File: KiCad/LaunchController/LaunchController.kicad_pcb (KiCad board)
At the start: 2 copper layers, 120 x 66 mm, 165 parts, among them J1 DC_IN, J10 CONN_EXT_UART, J11 CONN_EXT_I2C_0, J12 CONN_EXT_I2C_1, J13 CONN_EXT_I2C_2, J14 CONN_EXT_I2C_3, J15 CONN_EXT_SPI_0, J16 CONN_EXT_SPI_1, J17 CONN_EXT_SPI_2, J18 CONN_EXT_GPIO_0, J19 CONN_EXT_GPIO_1, J2 CONN_USB, J20 CONN_EXT_GPIO_2, J21 CONN_EXT_GPIO_3, J29 CONN_CONVERTER, J3 USB_B_Micro, J4 CONN_AUDIO, J5 CONN_SPEAKER, J6 CONN_ICSP, J7 L, J8 R, J9 RJ45, Q1 TJ8S06M3L, Q2 2SC3325-Y, Q3 TJ8S06M3L, SW1 SW_RESET, U1 FT232RL, U10 U74HC14, U2 24LC256, U3 INA219BIDCNT, U4 ATMEGA2560-16AUR, U5 INA219BIDCNT, U6 NJM7805SDL1, U7 LTC485CN8#PBF, U8 U74HC14, U9 U74HC14, Y1 HUSG-16.000-20

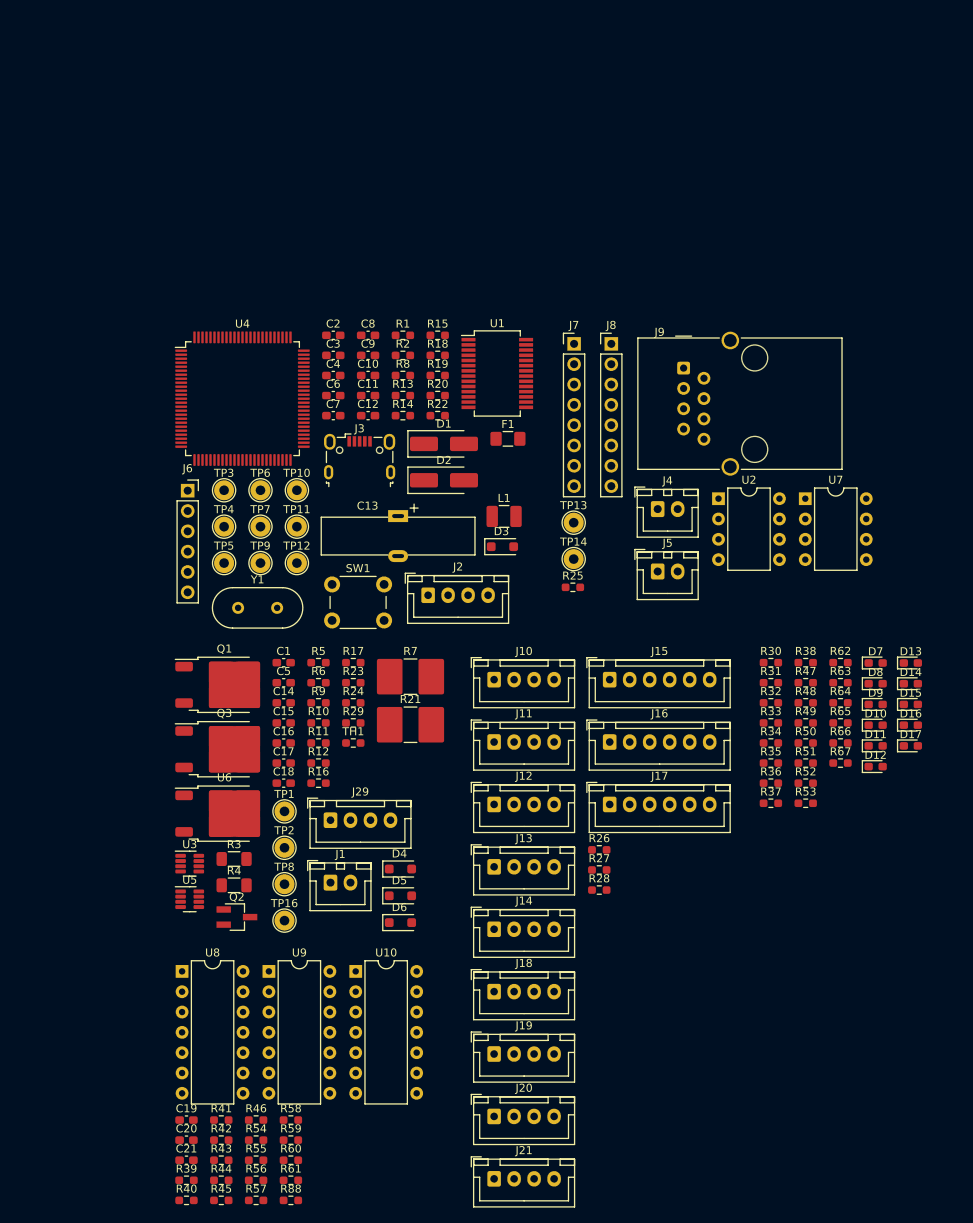
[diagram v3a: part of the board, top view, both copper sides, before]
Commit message: 端子台を選定
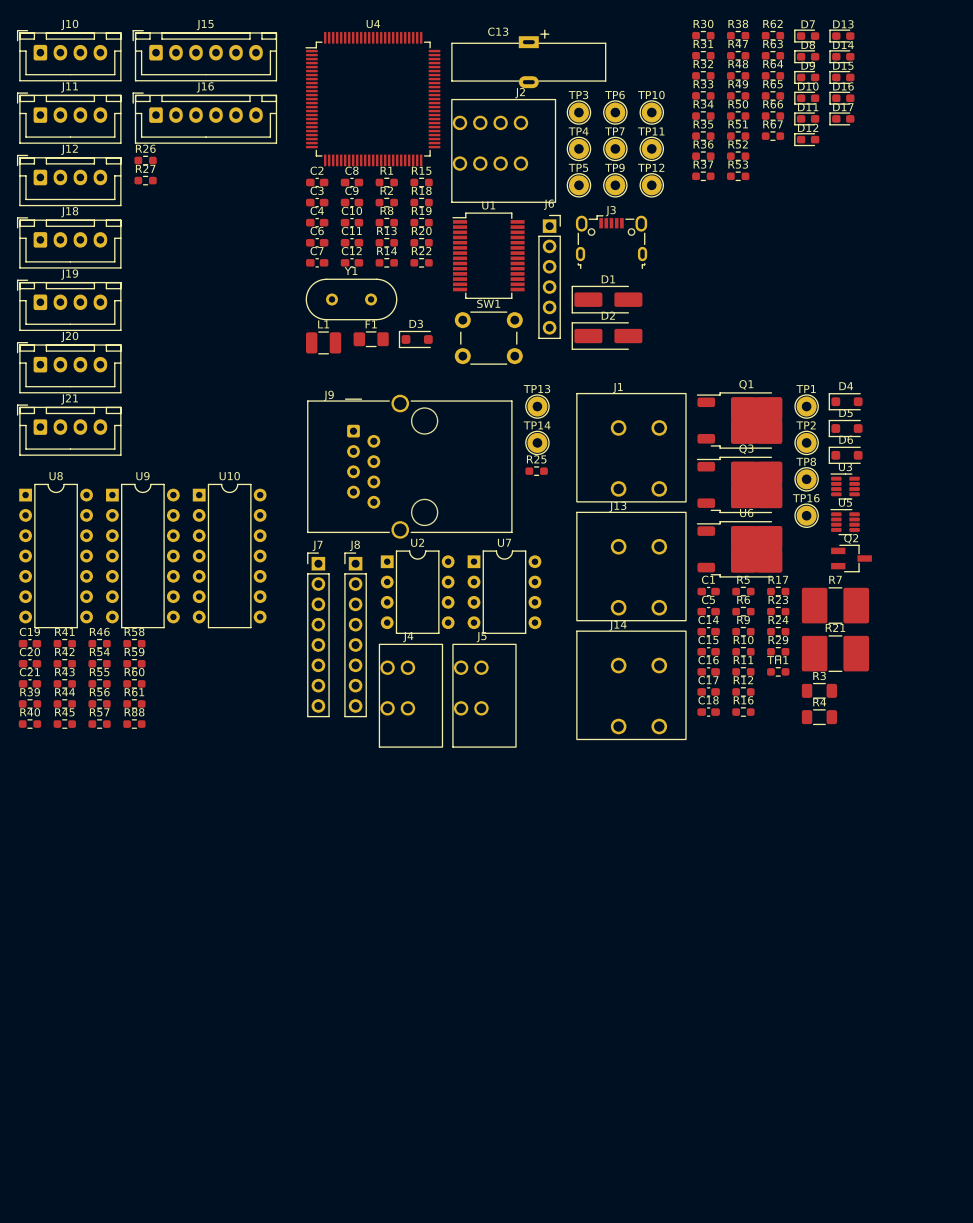
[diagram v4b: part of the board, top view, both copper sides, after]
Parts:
- removed J17: CONN_EXT_SPI_2, Connector_JST:JST_XH_B6B-XH-A_1x06_P2.50mm_Vertical
- removed J29: CONN_CONVERTER, Connector_JST:JST_XH_B4B-XH-A_1x04_P2.50mm_Vertical
- removed R28: 4.7kR, Resistor_SMD:R_0603_1608Metric_Pad0.98x0.95mm_HandSolder
- J1: footprint Connector_JST:JST_XH_B2B-XH-A_1x02_P2.50mm_Vertical -> TSRP_TerminalBlock_Alphaplus:TB411-2-2-E-1
- J13: value CONN_EXT_I2C_2 -> TO_CONVERTER; footprint Connector_JST:JST_XH_B4B-XH-A_1x04_P2.50mm_Vertical -> TSRP_TerminalBlock_Alphaplus:TB411-2-2-E-1
- J14: value CONN_EXT_I2C_3 -> FROM_CONVERTER; footprint Connector_JST:JST_XH_B4B-XH-A_1x04_P2.50mm_Vertical -> TSRP_TerminalBlock_Alphaplus:TB411-2-2-E-1
- J2: footprint Connector_JST:JST_XH_B4B-XH-A_1x04_P2.50mm_Vertical -> TSRP_TerminalBlock_Alphaplus:TB401-1-4-E
- J4, J5: footprint Connector_JST:JST_XH_B2B-XH-A_1x02_P2.50mm_Vertical -> TSRP_TerminalBlock_Alphaplus:TB401-1-2-E
- moved J21 109.8 mm to (-121.0, 98.2)
- moved J18 109.8 mm to (-121.0, 74.8)
- moved J20 109.8 mm to (-121.0, 90.4)
- moved J19 109.8 mm to (-121.0, 82.6)
- moved R26 103.2 mm to (-107.9, 64.9)
- moved R27 103.2 mm to (-107.9, 67.4)
- moved J10 96.7 mm to (-121.0, 51.4)
- moved J12 96.7 mm to (-121.0, 67.0)
- moved J15 96.7 mm to (-106.6, 51.4)
- moved J11 96.7 mm to (-121.0, 59.2)
- moved J16 96.7 mm to (-106.6, 59.2)
- moved U3 94.6 mm to (-20.4, 105.6)
- moved U5 94.6 mm to (-20.4, 110.1)
- moved Q2 88.9 mm to (-19.7, 114.6)
- moved TP16 82.6 mm to (-25.3, 109.3)
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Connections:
- J13 pad 2: I2C_SCL -> TO_CONVERTER
- J14 pad 2: I2C_SCL -> FROM_CONVERTER

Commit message: 拡張スロットを削除
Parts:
- removed J10: CONN_EXT_UART, Connector_JST:JST_XH_B4B-XH-A_1x04_P2.50mm_Vertical
- removed J11: CONN_EXT_I2C_0, Connector_JST:JST_XH_B4B-XH-A_1x04_P2.50mm_Vertical
- removed J12: CONN_EXT_I2C_1, Connector_JST:JST_XH_B4B-XH-A_1x04_P2.50mm_Vertical
- removed J15: CONN_EXT_SPI_0, Connector_JST:JST_XH_B6B-XH-A_1x06_P2.50mm_Vertical
- removed J16: CONN_EXT_SPI_1, Connector_JST:JST_XH_B6B-XH-A_1x06_P2.50mm_Vertical
- removed J18: CONN_EXT_GPIO_0, Connector_JST:JST_XH_B4B-XH-A_1x04_P2.50mm_Vertical
- removed J19: CONN_EXT_GPIO_1, Connector_JST:JST_XH_B4B-XH-A_1x04_P2.50mm_Vertical
- removed J20: CONN_EXT_GPIO_2, Connector_JST:JST_XH_B4B-XH-A_1x04_P2.50mm_Vertical
- removed J21: CONN_EXT_GPIO_3, Connector_JST:JST_XH_B4B-XH-A_1x04_P2.50mm_Vertical
- removed R26, R27: 4.7kR, Resistor_SMD:R_0603_1608Metric_Pad0.98x0.95mm_HandSolder
- added J17: CONN_STATUS_PANEL, TSRP_Connector_Hirose:DF51A-14DP-2DS, F.Cu at (-32.5, 81.2)
- added J22: CONN_PANEL_BAORD_2, TSRP_Connector_Hirose:DF51A-22DP-2DS, F.Cu at (-32.5, 54.3)
- added J23: CONN_PANEL_BAORD_1, TSRP_Connector_Hirose:DF51A-18DP-2DS, F.Cu at (-32.5, 67.8)
- moved U4 247.8 mm to (164.9, 98.2)
- moved R43 125.7 mm to (-39.3, 32.2)
- moved C21 125.7 mm to (-43.6, 32.2)
- moved R41 125.7 mm to (-39.3, 27.2)
- moved R42 125.7 mm to (-39.3, 29.7)
- moved R44 125.7 mm to (-39.3, 34.7)
- moved R45 125.7 mm to (-39.3, 37.3)
- moved R55 125.7 mm to (-34.9, 32.2)
- moved R60 125.7 mm to (-30.6, 32.2)
- moved C19 125.7 mm to (-43.6, 27.2)
- moved C20 125.7 mm to (-43.6, 29.7)
- moved R39 125.7 mm to (-43.6, 34.7)
- moved R40 125.7 mm to (-43.6, 37.3)
- moved R46 125.7 mm to (-34.9, 27.2)
- moved R54 125.7 mm to (-34.9, 29.7)
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
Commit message: 配線終わらん
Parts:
- removed C19, C20, C21: 0.1uF, Capacitor_SMD:C_0603_1608Metric_Pad1.08x0.95mm_HandSolder
- removed J7: L, Connector_PinHeader_2.54mm:PinHeader_1x08_P2.54mm_Vertical
- removed J8: R, Connector_PinHeader_2.54mm:PinHeader_1x08_P2.54mm_Vertical
- removed J9: RJ45, Connector_RJ:RJ45_Wuerth_7499010001A_Horizontal
- removed R39, R40, R41, R42, R43, R44, R45, R46, R54, R55, R56, R57, R58, R59, R60, R61, R88: 1kR, Resistor_SMD:R_0603_1608Metric_Pad0.98x0.95mm_HandSolder
- removed TP10: TP_SDA, TestPoint:TestPoint_THTPad_D2.5mm_Drill1.2mm
- removed TP11: TP_RX0, TestPoint:TestPoint_THTPad_D2.5mm_Drill1.2mm
- removed TP12: TP_TX0, TestPoint:TestPoint_THTPad_D2.5mm_Drill1.2mm
- removed TP13: TP_A, TestPoint:TestPoint_THTPad_D2.5mm_Drill1.2mm
- removed TP14: TP_B, TestPoint:TestPoint_THTPad_D2.5mm_Drill1.2mm
- removed TP3: TP_D+, TestPoint:TestPoint_THTPad_D2.5mm_Drill1.2mm
- removed TP4: TP_D-, TestPoint:TestPoint_THTPad_D2.5mm_Drill1.2mm
- removed TP5: TP_SCK, TestPoint:TestPoint_THTPad_D2.5mm_Drill1.2mm
- removed TP6: TP_MOSI, TestPoint:TestPoint_THTPad_D2.5mm_Drill1.2mm
- removed TP7: TP_MISO, TestPoint:TestPoint_THTPad_D2.5mm_Drill1.2mm
- removed TP9: TP_SCL, TestPoint:TestPoint_THTPad_D2.5mm_Drill1.2mm
- removed U10, U8, U9: U74HC14, Package_DIP:DIP-14_W7.62mm
- added G***: LOGO, LOGO, F.Cu at (136.2, 73.5)
- added G***: LOGO, LOGO, F.Cu at (92.7, 73.5)
- added J10: RJ45, Connector_RJ:RJ45_Wuerth_7499010001A_Horizontal, F.Cu at (95.0, 95.7)
- added U11: DFPlayer, TSRP_Module:DFPlayer-mini, F.Cu at (90.0, 114.1)
- J1, J13, J14, J17, J2, J22, J23, J4, J5: moved to B.Cu
- moved R53 290.5 mm to (176.2, 93.5), turned to 180 degrees
- moved R63 288.3 mm to (176.2, 98.7), turned to 180 degrees
- moved D14 279.1 mm to (176.2, 95.2), turned to 180 degrees
- moved D15 278.9 mm to (176.2, 97.0), turned to 180 degrees
- moved J1 277.2 mm to (173.8, 122.5), turned to 180 degrees
- moved TP2 270.8 mm to (190.7, 123.5)
- moved C1 262.1 mm to (178.7, 117.9), turned to 180 degrees
- moved C2 261.5 mm to (177.2, 88.0), turned to 180 degrees
- moved Q1 260.5 mm to (177.9, 106.8), turned to 90 degrees
- moved R49 260.2 mm to (145.4, 88.5)
- moved R51 259.9 mm to (145.4, 90.5)
- moved TP16 257.7 mm to (182.7, 118.0)
- moved J13 257.6 mm to (158.8, 122.5), turned to 180 degrees
- moved SW1 257.0 mm to (190.4, 110.7), turned to -90 degrees
- moved R65 255.6 mm to (145.4, 85.5)
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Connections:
- net CONN_LED_SAFTEY renamed LED_SAFTEY
- C8 pad 1: Net-(U4-AREF) -> USB_GND
- C8 pad 2: USB_GND -> Net-(U4-AREF)
- D3 pad 2: CTL_RESET -> SW_RESET
- J22 pad 11: CONN_LED_CLOSE -> LED_CLOSE
- J22 pad 13: CONN_LED_IGNITOR -> LED_IGNITOR
- J22 pad 15: CONN_LED_DUMP -> LED_DUMP
- J22 pad 17: CONN_LED_SHIFT -> LED_SHIFT
- J22 pad 19: CONN_LED_SEQUENCE -> LED_SEQUENCE
- J22 pad 21: CONN_LED_POWER -> LED_POWER
- J22 pad 9: CONN_LED_FB_SHIFT -> LED_FB_SHIFT
- Q2 pad 3: CTL_RUN -> SW_RUN
- R13 pad 2: CTL_RESET -> SW_RESET
- R4 pad 2: CTL_RUN -> SW_RUN
- SW1 pad 2: CTL_RESET -> SW_RESET
- U4 pad 25: unconnected-(U4-PB6-Pad25) -> CTL_POWER
- U4 pad 30: CTL_RESET -> SW_RESET
- U4 pad 35: unconnected-(U4-PL0-Pad35) -> LED_LOW_VOLTAGE
- U4 pad 36: unconnected-(U4-PL1-Pad36) -> LED_TASK
- U4 pad 37: unconnected-(U4-PL2-Pad37) -> LED_COM
- U4 pad 38: unconnected-(U4-PL3-Pad38) -> LED_CAUTION
- U4 pad 47: unconnected-(U4-PD4-Pad47) -> LED_POWER
- U4 pad 48: unconnected-(U4-PD5-Pad48) -> LED_SEQUENCE
- U4 pad 49: unconnected-(U4-PD6-Pad49) -> LED_SHIFT
- U4 pad 50: unconnected-(U4-PD7-Pad50) -> LED_DUMP
- U4 pad 51: unconnected-(U4-PG0-Pad51) -> LED_IGNITOR
- U4 pad 52: unconnected-(U4-PG1-Pad52) -> LED_CLOSE
- U4 pad 53: unconnected-(U4-PC0-Pad53) -> LED_FB_SHIFT
- U4 pad 90: unconnected-(U4-PF7-Pad90) -> LED_RS485_RX
- U4 pad 91: unconnected-(U4-PF6-Pad91) -> LED_RS485_TX
- U4 pad 92: unconnected-(U4-PF5-Pad92) -> CTL_RS485_DERE
- U4 pad 93: unconnected-(U4-PF4-Pad93) -> VREF_THERMISTOR
- U4 pad 94: unconnected-(U4-PF3-Pad94) -> VREF_12V
- U4 pad 95: unconnected-(U4-PF2-Pad95) -> VREF_VSW
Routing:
- net LED_5V: track 0.00 -> 362.9 mm, vias 0 -> 11
- net LED_INPUT: track 0.00 -> 160.4 mm, vias 0 -> 5
- net I2C_SCL: track 0.00 -> 147.8 mm, vias 0 -> 4
- net LED_12V: track 0.00 -> 132.5 mm, vias 0 -> 4
- net I2C_SDA: track 0.00 -> 128.8 mm, vias 0 -> 3
- net CTL_RESET: track 0.00 -> 91.0 mm, vias 0 -> 3
- net LED_USB_RX: track 0.00 -> 89.5 mm, vias 0 -> 3
- net LED_LOW_VOLTAGE: track 0.00 -> 86.1 mm, vias 0 -> 4
- net LED_USB_TX: track 0.00 -> 75.5 mm, vias 0 -> 3
- net CTL_POWER: track 0.00 -> 68.7 mm, vias 0 -> 2
- net USB_VBUS: track 0.00 -> 54.2 mm, vias 0 -> 2
- net UART1_RX: track 0.00 -> 53.1 mm, vias 0 -> 1
- net LED_CAUTION: track 0.00 -> 52.7 mm, vias 0 -> 5
- net VREF_THERMISTOR: track 0.00 -> 51.7 mm, vias 0 -> 4
- net Net-(U4-PE1): track 0.00 -> 51.5 mm, vias 0 -> 2
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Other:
- board text added: "+"
- board text added: "-"
- board text added: "12V"
- board text added: "5V"
- board text added: "AUDIO"
- board text added: "Com"
- board text added: "Ctn"
- board text added: "D+"
- board text added: "D-"
- board text added: "DC 15-24V 3.2A MAX"
- board text added: "DC IN"
- board text added: "FROM DCDC"
- board text added: "GND"
- board text added: "Gen 6 GSE Launch Controller Build 1"
- board text added: "ICSP"
- board text added: "INPUT"
- board text added: "LOW"
- board text added: "POWER"
- board text added: "RESET"
- board text added: "Rx"
- board text added: "SPEAKER"
- board text added: "TO DCDC"
- board text added: "Tokai Student Rocket Project"
- board text added: "Tsk"
- board text added: "Tx"
- board text added: "USB"
- board text added: "VBUS"

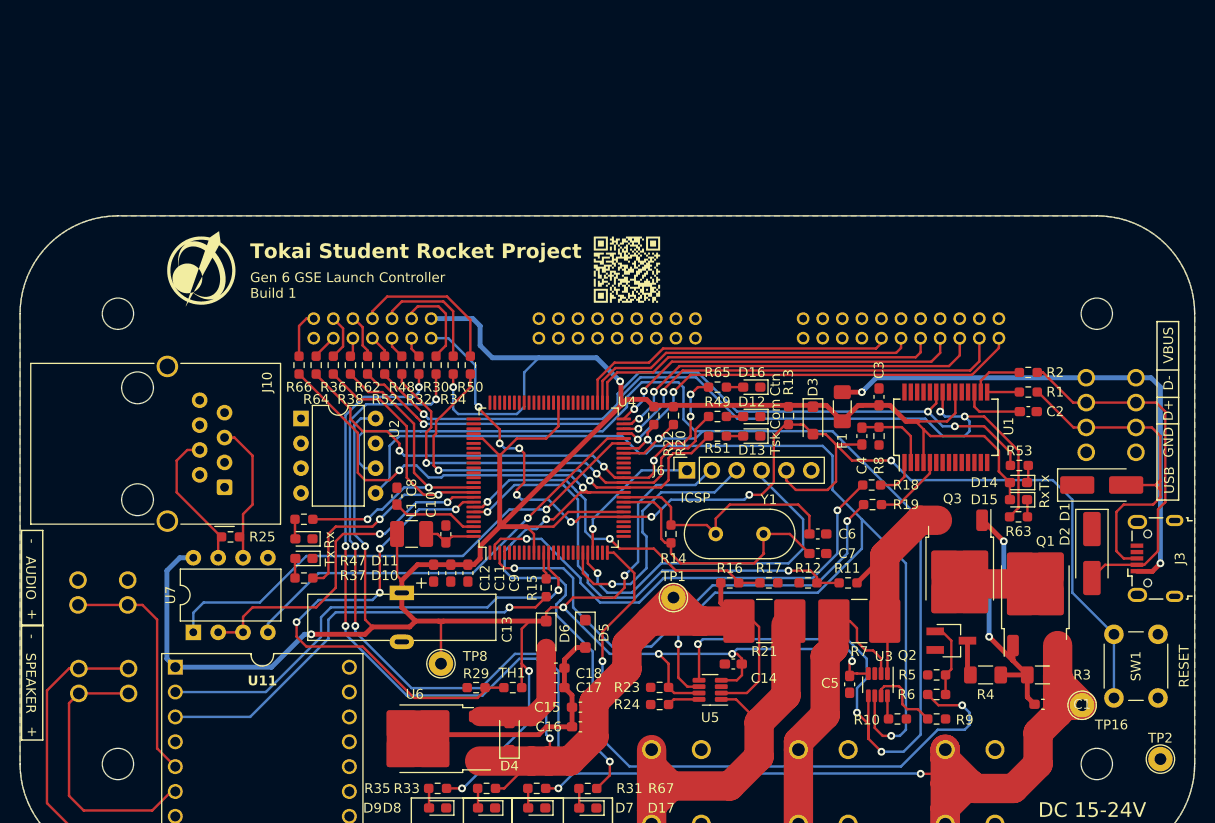
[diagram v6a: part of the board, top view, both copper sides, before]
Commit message: シュミットトリガー無しで部品を配置
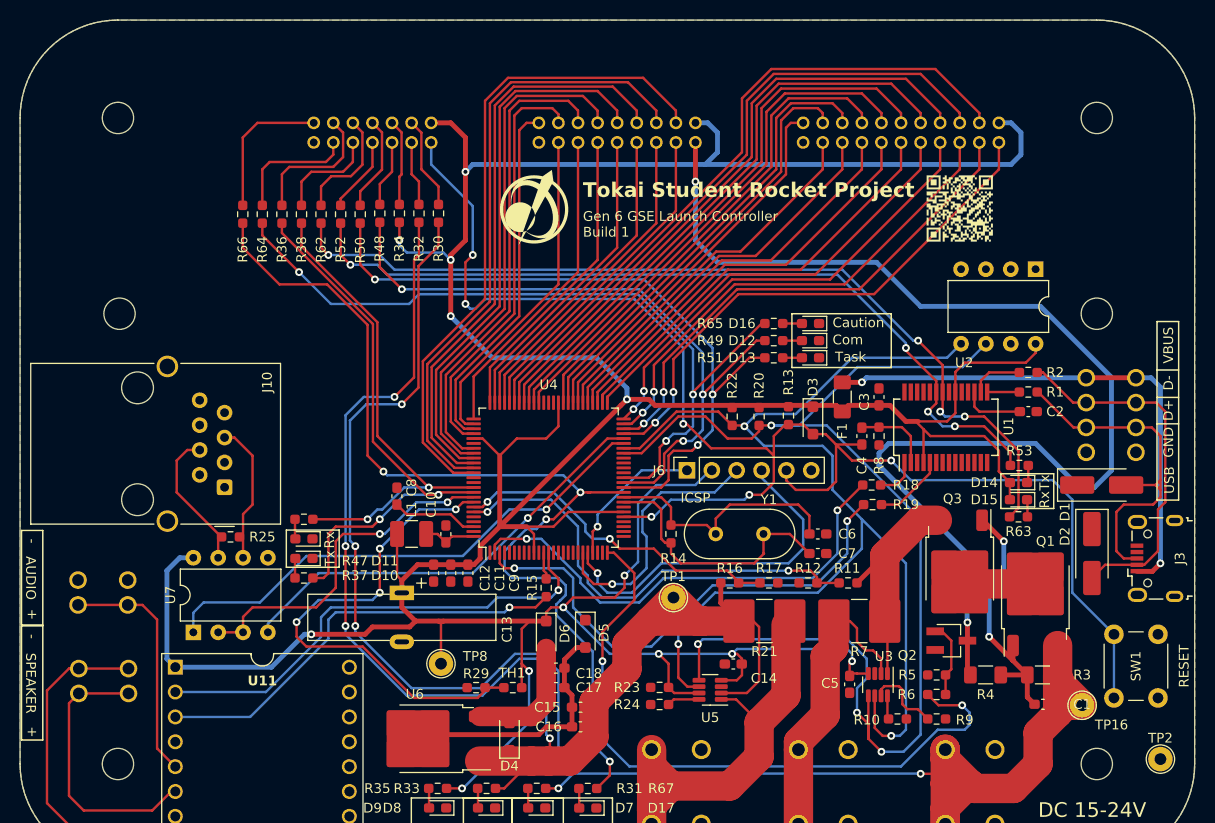
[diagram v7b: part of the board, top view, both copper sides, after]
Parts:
- added REF**: MountingHole_3.2mm_M3, MountingHole:MountingHole_3.2mm_M3, F.Cu at (184.2, 78.0)
- added REF**: MountingHole_3.2mm_M3, MountingHole:MountingHole_3.2mm_M3, F.Cu at (84.3, 78.0)
- moved U2 76.6 mm to (177.9, 73.4), turned to -90 degrees
- moved G*** 34.6 mm to (170.2, 67.2)
- moved G*** 34.6 mm to (126.7, 67.2)
- moved J17 20.0 mm to (104.2, 60.5)
- moved J22 20.0 mm to (154.2, 60.5)
- moved J23 20.0 mm to (127.2, 60.5)
- moved REF** 20.0 mm to (184.2, 58.0)
- moved REF** 20.0 mm to (84.2, 58.0)
- moved R50 19.1 mm to (108.9, 67.8)
- moved R66 16.5 mm to (96.9, 67.8)
- moved R34 16.4 mm to (112.9, 67.7)
- moved R64 16.4 mm to (98.9, 67.8)
- moved R36 16.3 mm to (100.9, 67.8)
- moved R38 16.2 mm to (102.9, 67.8)
- moved R62 16.1 mm to (104.9, 67.8)
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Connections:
- C4 pad 2: CTL_RESET -> SW_RESET
- J22 pad 10: CONN_LED_PURGE -> LED_PURGE
- J22 pad 12: CONN_LED_OPEN -> LED_OPEN
- J22 pad 14: CONN_LED_O2 -> LED_O2
- J22 pad 16: CONN_LED_FILL -> LED_FILL
- J22 pad 18: CONN_LED_EMERGENCY -> LED_EMERGENCY
- J22 pad 2: CONN_LED_FB_PURGE -> LED_FB_PURGE
- J22 pad 3: CONN_LED_FB_CLOSE -> LED_FB_CLOSE
- J22 pad 4: CONN_LED_FB_OPEN -> LED_FB_OPEN
- J22 pad 5: CONN_LED_FB_IGNITOR -> LED_FB_IGNITOR
- J22 pad 6: CONN_FB_LED_O2 -> LED_FB_O2
- J22 pad 7: CONN_LED_FB_DUMP -> LED_FB_DUMP
- J22 pad 8: CONN_LED_FB_FILL -> LED_FB_FILL
- J6 pad 5: CTL_RESET -> SW_RESET
- U4 pad 54: unconnected-(U4-PC1-Pad54) -> LED_FB_DUMP
- U4 pad 55: unconnected-(U4-PC2-Pad55) -> LED_FB_IGNITOR
- U4 pad 56: unconnected-(U4-PC3-Pad56) -> LED_FB_CLOSE
- U4 pad 57: unconnected-(U4-PC4-Pad57) -> LED_FB_PURGE
- U4 pad 58: unconnected-(U4-PC5-Pad58) -> LED_FB_OPEN
- U4 pad 59: unconnected-(U4-PC6-Pad59) -> LED_FB_O2
- U4 pad 60: unconnected-(U4-PC7-Pad60) -> LED_FB_FILL
- U4 pad 65: unconnected-(U4-PJ2-Pad65) -> LED_PURGE
- U4 pad 66: unconnected-(U4-PJ3-Pad66) -> LED_OPEN
- U4 pad 67: unconnected-(U4-PJ4-Pad67) -> LED_O2
- U4 pad 68: unconnected-(U4-PJ5-Pad68) -> LED_FILL
- U4 pad 69: unconnected-(U4-PJ6-Pad69) -> LED_EMERGENCY
- U4 pad 70: unconnected-(U4-PG2-Pad70) -> LED_SAFTEY
- U4 pad 71: unconnected-(U4-PA7-Pad71) -> SW_SAFETY
- U4 pad 72: unconnected-(U4-PA6-Pad72) -> SW_EMERGENCY_STOP
- U4 pad 73: unconnected-(U4-PA5-Pad73) -> SW_CONFIRM_2
- U4 pad 74: unconnected-(U4-PA4-Pad74) -> SW_SHIFT
- U4 pad 75: unconnected-(U4-PA3-Pad75) -> SW_DUMP
- U4 pad 76: unconnected-(U4-PA2-Pad76) -> SW_IGNITOR
- U4 pad 77: unconnected-(U4-PA1-Pad77) -> SW_CLOSE
- U4 pad 78: unconnected-(U4-PA0-Pad78) -> SW_PURGE
- U4 pad 79: unconnected-(U4-PJ7-Pad79) -> SW_OPEN
- U4 pad 82: unconnected-(U4-PK7-Pad82) -> SW_O2
- U4 pad 83: unconnected-(U4-PK6-Pad83) -> SW_FILL
- U4 pad 84: unconnected-(U4-PK5-Pad84) -> SW_CONFIRM_3
- U4 pad 85: unconnected-(U4-PK4-Pad85) -> SW_CONFIRM_1
- U4 pad 86: unconnected-(U4-PK3-Pad86) -> SW_SEQUENCE_START
- U4 pad 87: unconnected-(U4-PK2-Pad87) -> SW_KILL
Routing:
- net SW_RESET: track 34.3 -> 153.4 mm, vias 5 -> 6
- net SW_RUN: track 3.62 -> 121.1 mm, vias 0 -> 2
- net CTL_RESET: track 91.0 -> 0.00 mm, vias 3 -> 0
- net LED_SAFTEY: track 0.00 -> 69.1 mm
- net SW_KILL: track 0.00 -> 67.1 mm
- net LED_5V: track 362.9 -> 429.9 mm, vias 11 -> 13
- net LED_EMERGENCY: track 0.00 -> 66.0 mm
- net SW_SEQUENCE_START: track 0.00 -> 63.3 mm
- net LED_FILL: track 0.00 -> 63.0 mm
- net LED_O2: track 0.00 -> 59.9 mm
- net SW_CONFIRM_1: track 0.00 -> 59.5 mm
- net LED_OPEN: track 0.00 -> 56.8 mm
- net SW_CONFIRM_3: track 0.00 -> 55.8 mm
- net LED_PURGE: track 0.00 -> 53.7 mm
- net SW_FILL: track 0.00 -> 52.0 mm
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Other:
- board size 120 x 66 mm -> 120 x 86 mm
- board text added: "Caution"
- board text added: "Task"
- board text removed: "Ctn"
- board text removed: "Tsk"
